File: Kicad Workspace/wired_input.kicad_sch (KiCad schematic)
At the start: 1 part, among them U2 PCM1862DBT

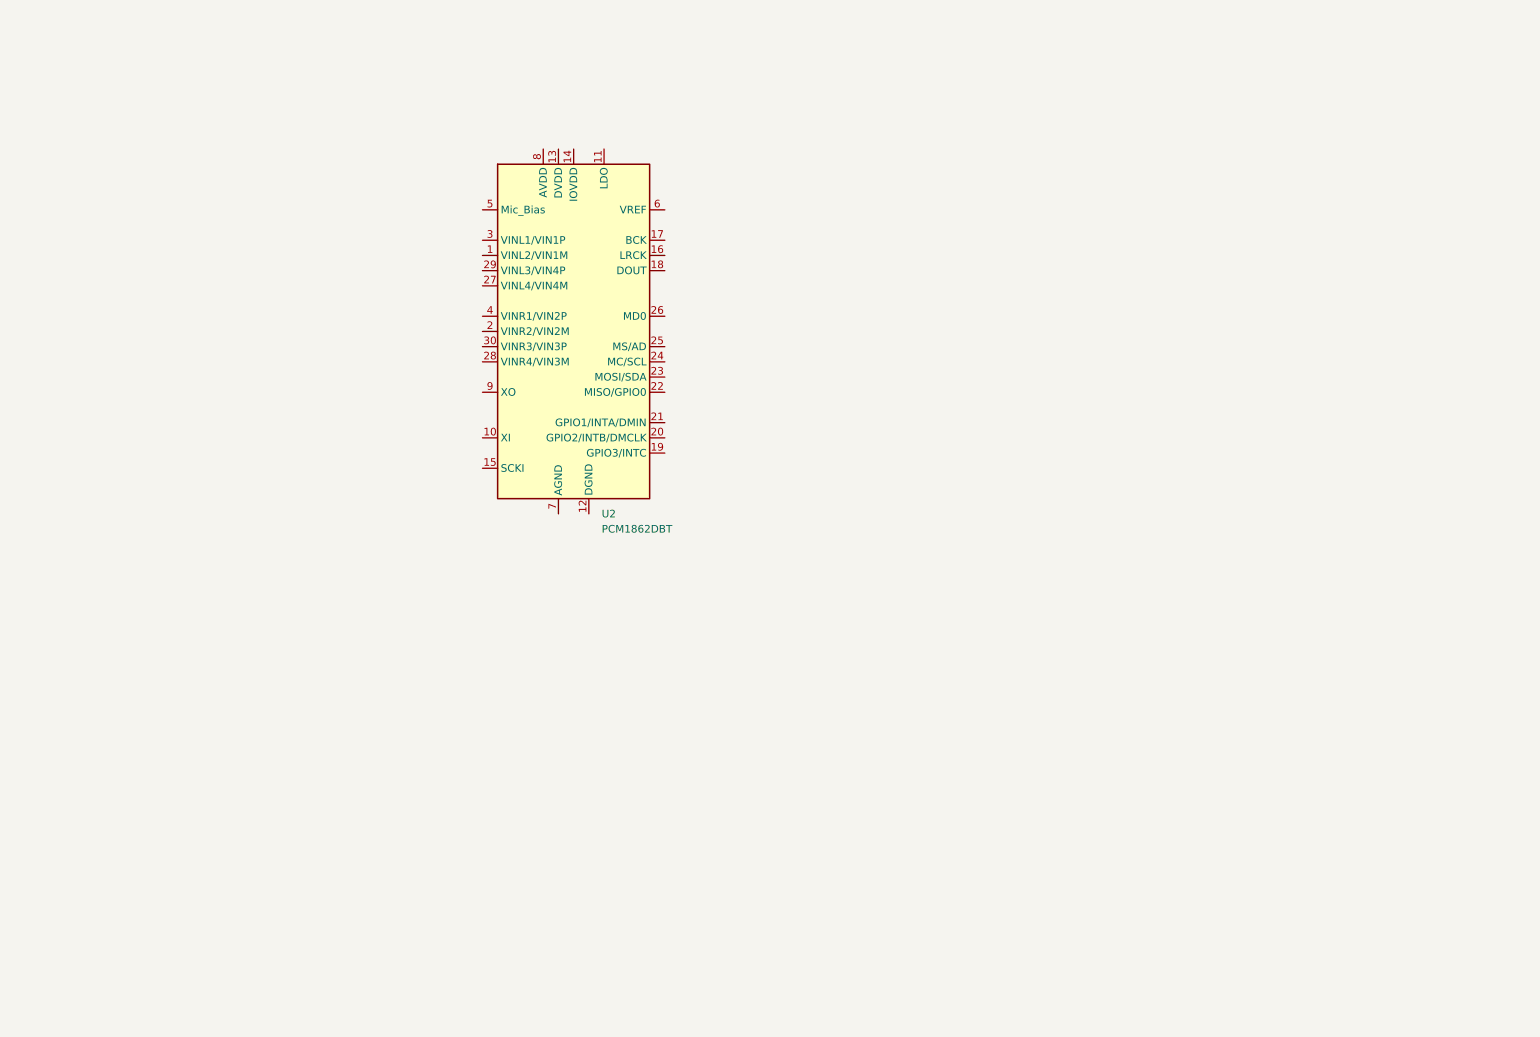
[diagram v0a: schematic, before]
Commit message: Wire input (ADC) schematics done
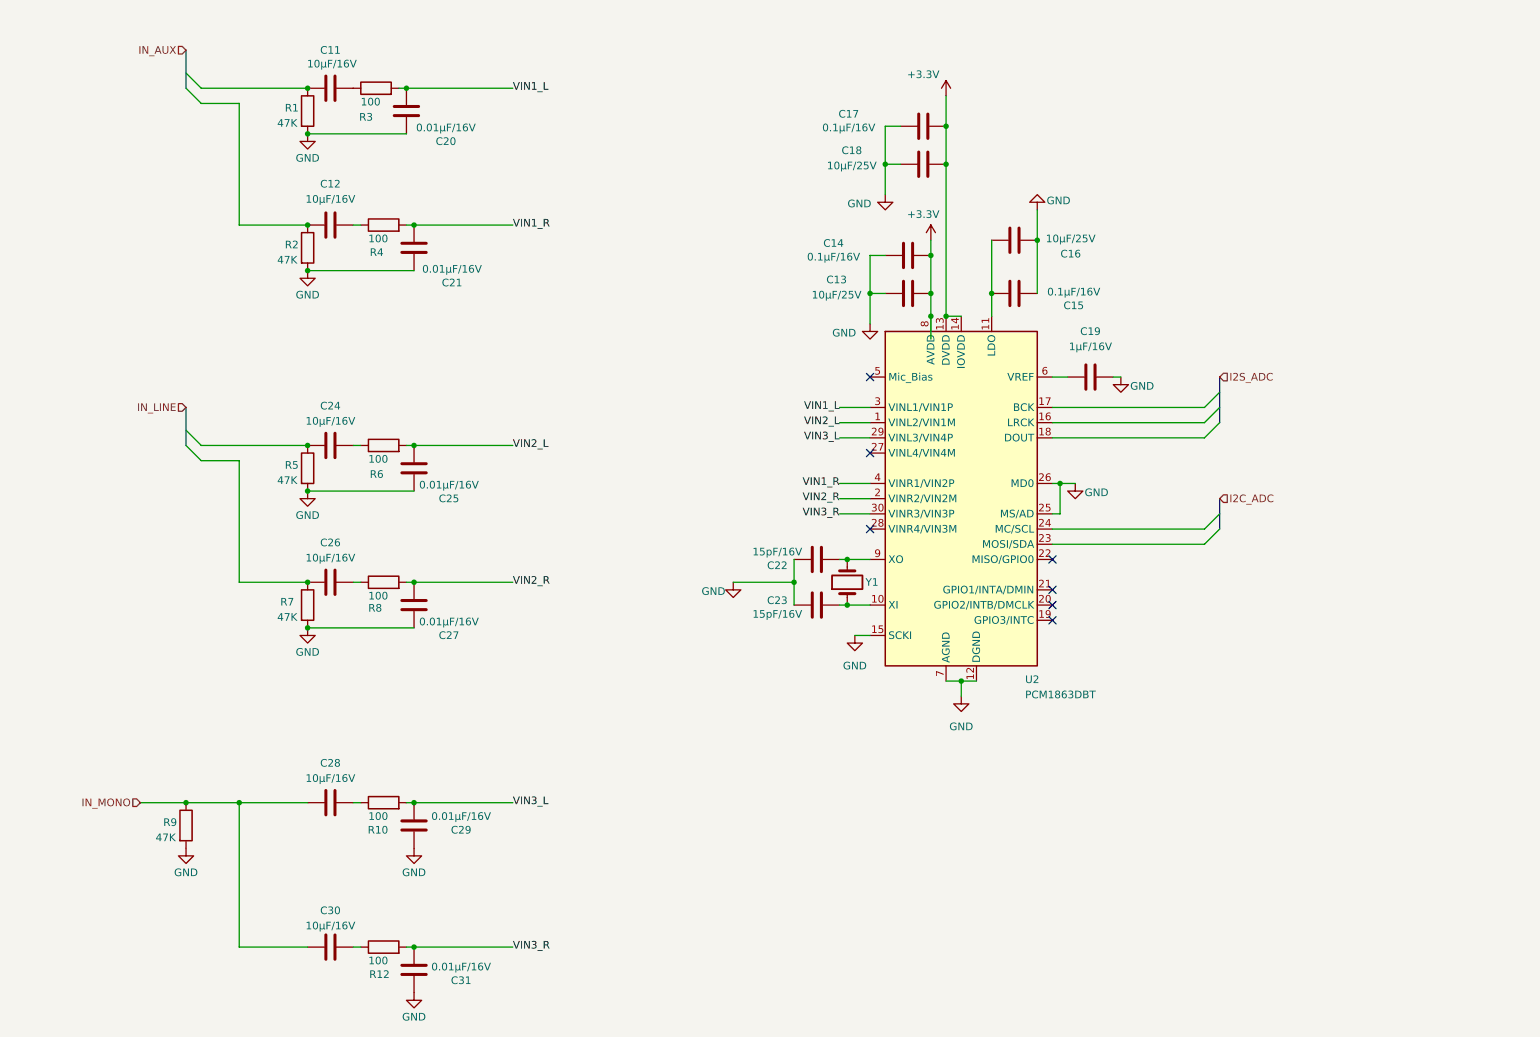
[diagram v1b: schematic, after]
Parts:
- added C11, C12, C24, C26, C28, C30: 10µF/16V, Capacitor_SMD:C_0805_2012Metric, symbol Device:C
- added C13, C16, C18: 10µF/25V, Capacitor_SMD:C_0805_2012Metric, symbol Device:C
- added C14, C15, C17: 0.1µF/16V, Capacitor_SMD:C_0402_1005Metric, symbol Device:C
- added C19: 1µF/16V, Capacitor_SMD:C_0805_2012Metric, symbol Device:C
- added C20, C21, C25, C27, C29, C31: 0.01µF/16V, Capacitor_SMD:C_0402_1005Metric, symbol Device:C
- added C22, C23: 15pF/16V, Capacitor_SMD:C_0402_1005Metric, symbol Device:C
- added R1, R2, R5, R7, R9: 47K, Resistor_SMD:R_01005_0402Metric, symbol Device:R
- added R10, R12, R3, R4, R6, R8: 100, Resistor_SMD:R_01005_0402Metric, symbol Device:R
- added Y1: Crystal, symbol Device:Crystal
- U2: value PCM1862DBT -> PCM1863DBT
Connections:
- net VIN2_L: now reaches U2.1 (VINL2/VIN1M)
- net VIN2_L: now also C25.1, R6.2
- net at U2.10 (XI): now also C23.2, Y1.1
- net at U2.11 (LDO): now also C15.1, C16.1
- net GND: now reaches U2.12 (DGND)
- net GND: now also U2.15 (SCKI), U2.25 (MS/AD), U2.26 (MD0), U2.7 (AGND), C13.2, C14.2, C15.2, C16.2, C17.2, C18.2, C19.2, C20.2, C21.2, C22.2, C23.1, C25.2, C27.2, C29.2, C31.2, R1.2, R2.2, R5.2, R7.2, R9.2
- net +3.3V: now reaches U2.13 (DVDD)
- net +3.3V: now also U2.14 (IOVDD), U2.8 (AVDD), C13.1, C14.1, C17.1, C18.1
- net VIN2_R: now reaches U2.2 (VINR2/VIN2M)
- net VIN2_R: now also C27.1, R8.2
- net VIN3_L: now reaches U2.29 (VINL3/VIN4P)
- net VIN3_L: now also C29.1, R10.2
- net VIN1_L: now reaches U2.3 (VINL1/VIN1P)
- net VIN1_L: now also C20.1, R3.2
- net VIN3_R: now reaches U2.30 (VINR3/VIN3P)
- net VIN3_R: now also C31.1, R12.2
- net VIN1_R: now reaches U2.4 (VINR1/VIN2P)
- net VIN1_R: now also C21.1, R4.2
- net at U2.6 (VREF): now also C19.1
- net at U2.9 (XO): now also C22.1, Y1.2
- new net: C26.2, R8.1
- new net: C28.2, R10.1
- new net: C11.2, R3.1
- new net: C26.1, R7.1
- new net: C12.1, R2.1
- new net: C12.2, R4.1
- new net: C30.2, R12.1
- new net: C11.1, R1.1
- new net: C24.2, R6.1
- new net: C24.1, R5.1
- new net IN_MONO: C28.1, C30.1, R9.1
- no-connect marks 0 -> 7
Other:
- moved on the sheet: U2

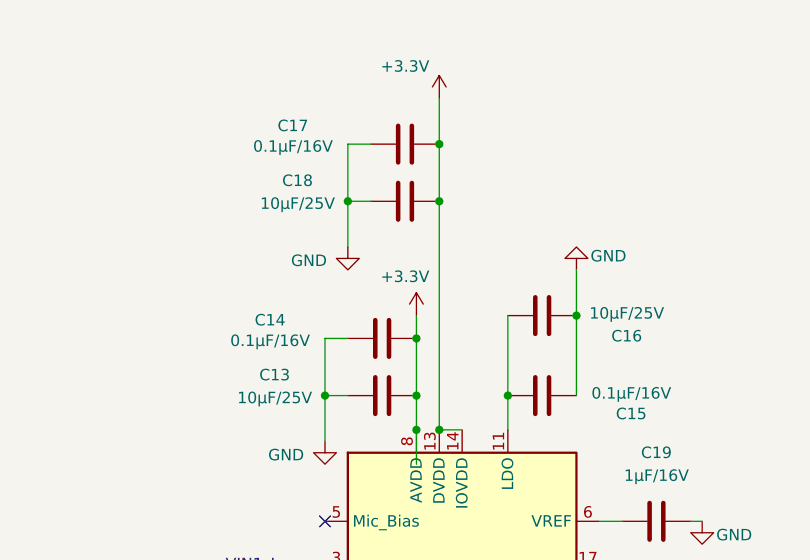
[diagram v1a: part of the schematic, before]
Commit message: fix: split analog 3.3 from digital 3.3
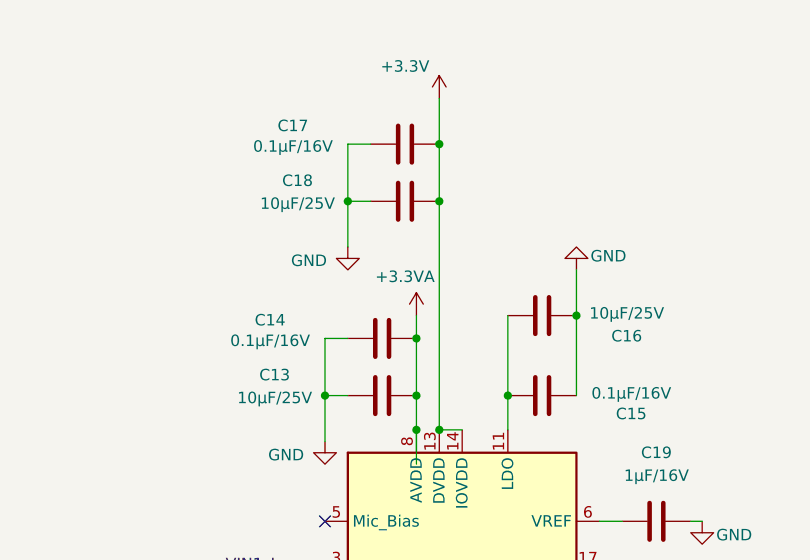
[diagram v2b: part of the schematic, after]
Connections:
- net +3.3V: no longer C13.1, C14.1, U2.8 (AVDD)
- new net +3.3VA: C13.1, C14.1, U2.8 (AVDD)
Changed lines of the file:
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@@
 			)
 		)
-		(property "Value" "+3.3V"
+		(property "Value" "+3.3VA"
 			(at 175.26 52.832 0)
 			(show_name no)

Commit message: feat: schematics almost done, starting to correct compile pb
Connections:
- net WIRE_LRCK: now reaches U2.16 (LRCK)
- net WIRE_BCK: now reaches U2.17 (BCK)
- net WIRE_DATA: now reaches U2.18 (DOUT)
- net SDA: now reaches U2.23 (MOSI/SDA)
- net SCL: now reaches U2.24 (MC/SCL)
- net IN_MONO renamed MONO
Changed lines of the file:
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@@
-	)
-	(bus_entry
-		(at 222.25 105.41)
-		(size 2.54 -2.54)
-		(stroke
-			(width 0)
-			(type default)
-		)
 	)
 	(bus_entry
@@
 	)
 	(bus_entry
-		(at 222.25 107.95)
-		(size 2.54 -2.54)
-		(stroke
-			(width 0)
-			(type default)
-		)
-	)
-	(bus_entry
 		(at 54.61 93.98)
 		(size -2.54 -2.54)
@@
 		)
 	)
+	(bus
+		(pts
+			(xy 222.25 102.87) (xy 222.25 107.95)
+		)
+		(stroke
+			(width 0)
+			(type default)
+		)
+	)
 	(wire
 		(pts
@@
 		(pts
 			(xy 179.07 69.85) (xy 181.61 69.85)
-		)
-		(stroke
-			(width 0)
-			(type default)
-		)
-	)
-	(bus
-		(pts
-			(xy 224.79 100.33) (xy 224.79 105.41)
 		)
 		(stroke
@@
 		)
 	)
+	(label "WIRE_BCK"
+		(at 212.09 85.09 0)
+		(effects
+			(font
+				(size 1.27 1.27)
+			)
+			(justify left bottom)
+		)
+	)
 	(label "VIN3_R"
 		(at 106.68 175.26 0)
@@
 		)
 	)
+	(label "SDA"
+		(at 217.17 107.95 0)
+		(effects
+			(font
+				(size 1.27 1.27)
+			)
+			(justify left bottom)
+		)
+	)
+	(label "SCL"
+		(at 217.17 105.41 0)
+		(effects
+			(font
+				(size 1.27 1.27)
+			)
+			(justify left bottom)
+		)
+	)
 	(label "VIN1_R"
 		(at 106.68 54.61 0)
@@
 		)
 	)
+	(label "WIRE_DATA"
+		(at 211.9659 90.17 0)
+		(effects
+			(font
+				(size 1.27 1.27)
+			)
+			(justify left bottom)
+		)
+	)
 	(label "VIN2_R"
 		(at 106.68 114.3 0)
@@
 		)
 	)
+	(label "WIRE_LRCK"
+		(at 212.09 87.63 0)
+		(effects
+			(font
+				(size 1.27 1.27)
+			)
+			(justify left bottom)
+		)
+	)
 	(label "VIN3_L"
 		(at 161.29 90.17 180)
@@
 		)
 	)
-	(hierarchical_label "IN_MONO"
+	(hierarchical_label "I2C{SCL SDA}"
+		(shape bidirectional)
+		(at 222.25 102.87 0)
+		(effects
+			(font
+				(size 1.27 1.27)
+			)
+			(justify left)
+		)
+	)
+	(hierarchical_label "MONO"
 		(shape input)
 		(at 44.45 151.13 180)
@@
 		)
 	)
-	(hierarchical_label "IN_AUX"
+	(hierarchical_label "AUX"
 		(shape input)
 		(at 52.07 25.4 180)
@@
 		)
 	)
-	(hierarchical_label "I2S_ADC"
-		(shape input)
+	(hierarchical_label "WIRE_I2S{WIRE_DATA WIRE_BCK WIRE_LRCK}"
+		(shape output)
 		(at 224.79 80.01 0)
 		(effects
@@
 		)
 	)
-	(hierarchical_label "I2C_ADC"
-		(shape input)
-		(at 224.79 100.33 0)
-		(effects
-			(font
-				(size 1.27 1.27)
-			)
-			(justify left)
-		)
-	)
-	(hierarchical_label "IN_LINE"
+	(hierarchical_label "LINE"
 		(shape input)
 		(at 52.07 85.09 180)

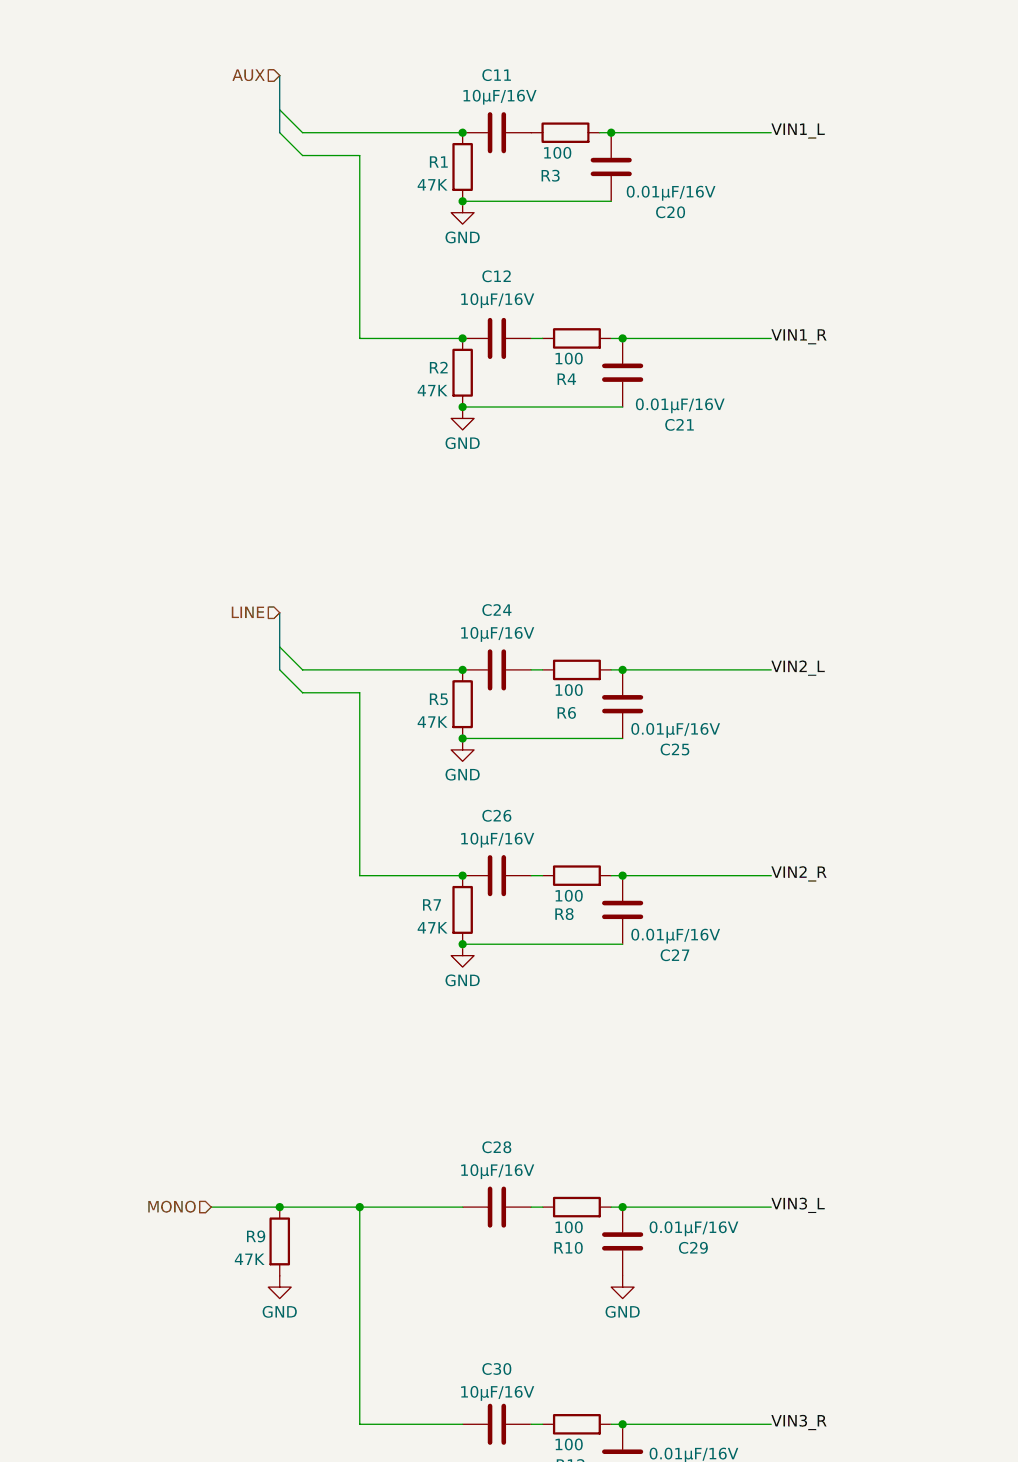
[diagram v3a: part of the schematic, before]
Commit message: feat: adding jack connectors on PCB
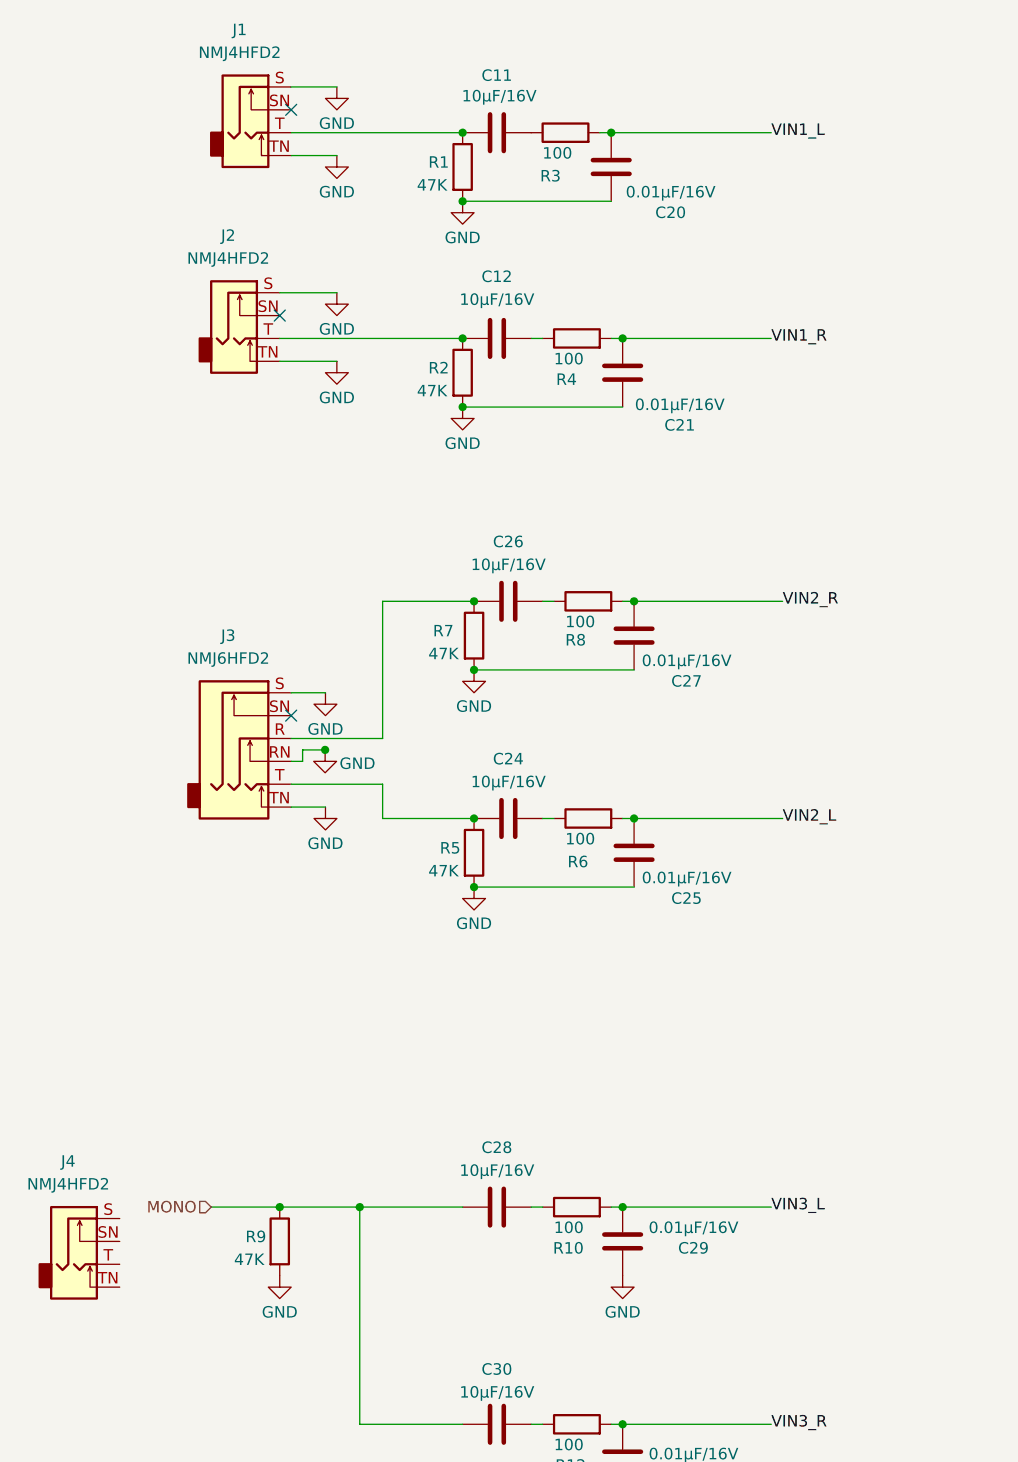
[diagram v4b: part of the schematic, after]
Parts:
- added J1, J2, J4: NMJ4HFD2, Connector_Audio:Jack_6.35mm_Neutrik_NMJ4HFD2_Horizontal, symbol Connector_Audio:NMJ4HFD2
- added J3: NMJ6HFD2, Connector_Audio:Jack_6.35mm_Neutrik_NMJ6HFD2_Horizontal, symbol Connector_Audio:NMJ6HFD2
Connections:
- net GND: now also J1.S, J1.TN, J2.S, J2.TN, J3.RN, J3.S, J3.TN
- net at C26.1, R7.1: now also J3.R
- net at C12.1, R2.1: now also J2.T
- net at C11.1, R1.1: now also J1.T
- net at C24.1, R5.1: now also J3.T
- no-connect marks 7 -> 10
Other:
- moved on the sheet: C24, C25, C26, C27, R5, R6, R7, R8

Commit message: feat: jack schematics
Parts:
- removed J3: NMJ6HFD2, Connector_Audio:Jack_6.35mm_Neutrik_NMJ6HFD2_Horizontal, symbol Connector_Audio:NMJ6HFD2
- added J3: AudioJack3_Switch, Connector_Audio:Jack_3.5mm_CUI_SJ1-3535NG_Horizontal, symbol Connector_Audio:AudioJack3_Switch
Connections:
- net MONO is gone; now on an unnamed net: C28.1, C30.1, R9.1
- net GND: now also J4.S, J4.TN, J3.RN, J3.S, J3.TN
- net at C26.1, R7.1: now also J3.R
- net at C24.1, R5.1: now also J3.T
- no-connect marks 10 -> 11
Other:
- moved on the sheet: C28, C29, C30, C31, J4, R10, R12, R9

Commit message: fix: Bus fix with correct syntax
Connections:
- net SCL renamed I2C.SCL
- net SDA renamed I2C.SDA
- net WIRE_BCK renamed WIRE_I2S.BCK
- net WIRE_DATA renamed WIRE_I2S.DATA
- net WIRE_LRCK renamed WIRE_I2S.LRCK
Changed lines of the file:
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@@
+	)
+	(bus_entry
+		(at 222.25 107.95)
+		(size 2.54 -2.54)
+		(stroke
+			(width 0)
+			(type default)
+		)
 	)
 	(bus_entry
@@
 		)
 	)
+	(bus_entry
+		(at 222.25 105.41)
+		(size 2.54 -2.54)
+		(stroke
+			(width 0)
+			(type default)
+		)
+	)
 	(wire
 		(pts
@@
 	(bus
 		(pts
-			(xy 222.25 102.87) (xy 222.25 107.95)
+			(xy 224.79 100.33) (xy 224.79 105.41)
 		)
 		(stroke
@@
 		)
 	)
-	(label "WIRE_BCK"
+	(label "WIRE_I2S.BCK"
 		(at 212.09 85.09 0)
 		(effects
@@
 		)
 	)
-	(label "SDA"
-		(at 217.17 107.95 0)
+	(label "I2C.SDA"
+		(at 213.36 107.95 0)
 		(effects
 			(font
@@
 		)
 	)
-	(label "SCL"
-		(at 217.17 105.41 0)
+	(label "I2C.SCL"
+		(at 213.36 105.41 0)
 		(effects
 			(font
@@
 		)
 	)
-	(label "WIRE_DATA"
-		(at 211.9659 90.17 0)
+	(label "WIRE_I2S.DATA"
+		(at 212.09 90.17 0)
 		(effects
 			(font
@@
 		)
 	)
-	(label "WIRE_LRCK"
+	(label "WIRE_I2S.LRCK"
 		(at 212.09 87.63 0)
 		(effects
@@
 	(hierarchical_label "I2C{SCL SDA}"
 		(shape bidirectional)
-		(at 222.25 102.87 0)
+		(at 224.79 100.33 0)
 		(effects
 			(font
@@
 		)
 	)
-	(hierarchical_label "WIRE_I2S{WIRE_DATA WIRE_BCK WIRE_LRCK}"
+	(hierarchical_label "WIRE_I2S{DATA BCK LRCK}"
 		(shape output)
 		(at 224.79 80.01 0)
